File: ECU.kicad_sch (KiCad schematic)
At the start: 6 parts

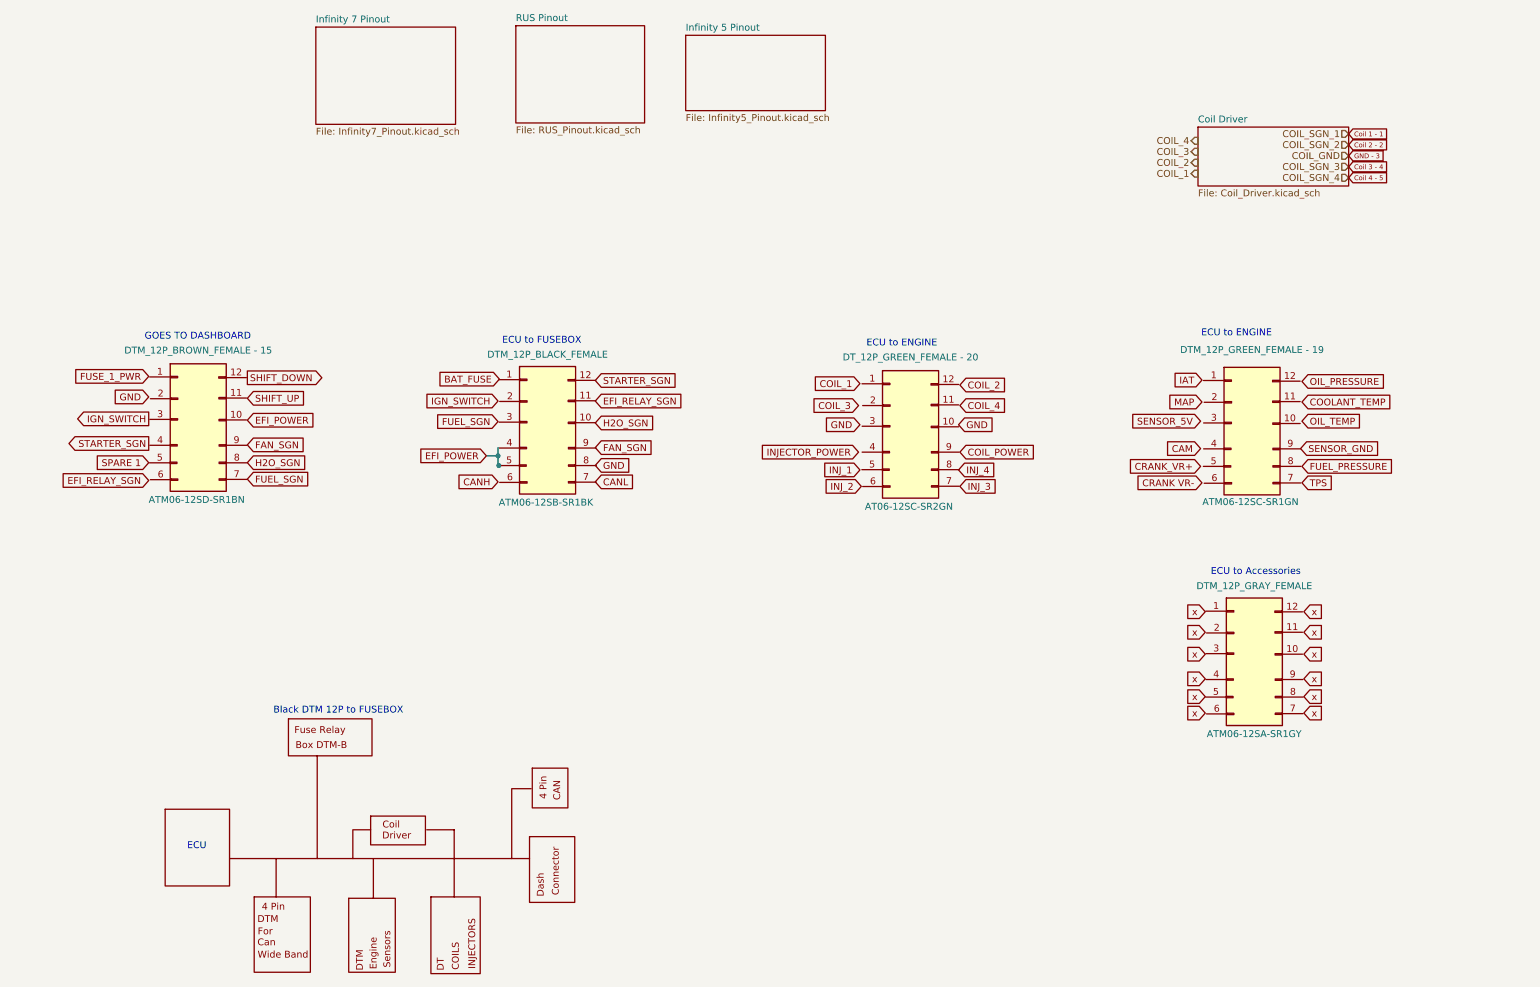
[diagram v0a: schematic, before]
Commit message: readd all connectors
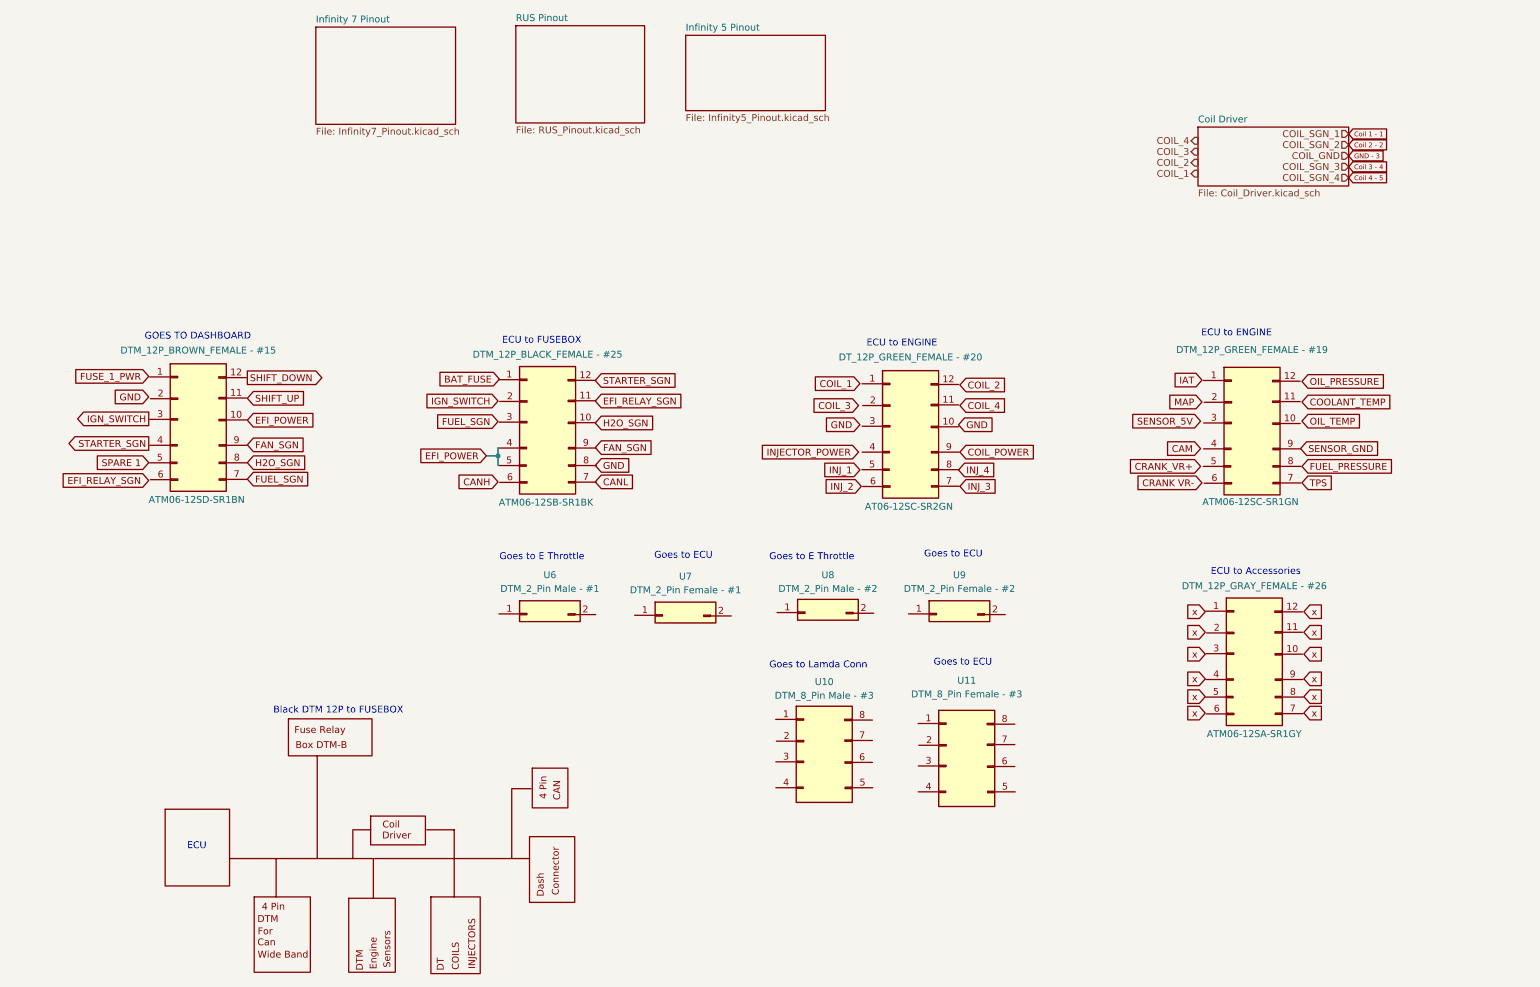
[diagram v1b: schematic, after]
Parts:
- added U10: DTM_8_Pin Male - #3, symbol SCR23 Library:DTM_8_Pin
- added U11: DTM_8_Pin Female - #3, symbol SCR23 Library:DTM_8_Pin
- added U6: DTM_2_Pin Male - #1, symbol SCR23 Library:DTM_2_Pin
- added U7: DTM_2_Pin Female - #1, symbol SCR23 Library:DTM_2_Pin
- added U8: DTM_2_Pin Male - #2, symbol SCR23 Library:DTM_2_Pin
- added U9: DTM_2_Pin Female - #2, symbol SCR23 Library:DTM_2_Pin
- U?: value DTM_12P_BROWN_FEMALE - 15 -> DTM_12P_BROWN_FEMALE - #15
- U?: value DTM_12P_GRAY_FEMALE -> DTM_12P_GRAY_FEMALE - #26
- U?: value DTM_12P_BLACK_FEMALE -> DTM_12P_BLACK_FEMALE - #25
- U?: value DTM_12P_GREEN_FEMALE - 19 -> DTM_12P_GREEN_FEMALE - #19
- U?: value DT_12P_GREEN_FEMALE - 20 -> DT_12P_GREEN_FEMALE - #20
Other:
- note added: "Goes to E Throttle"
- note added: "Goes to ECU"
- note added: "Goes to Lamda Conn"

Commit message: Updating Connectors
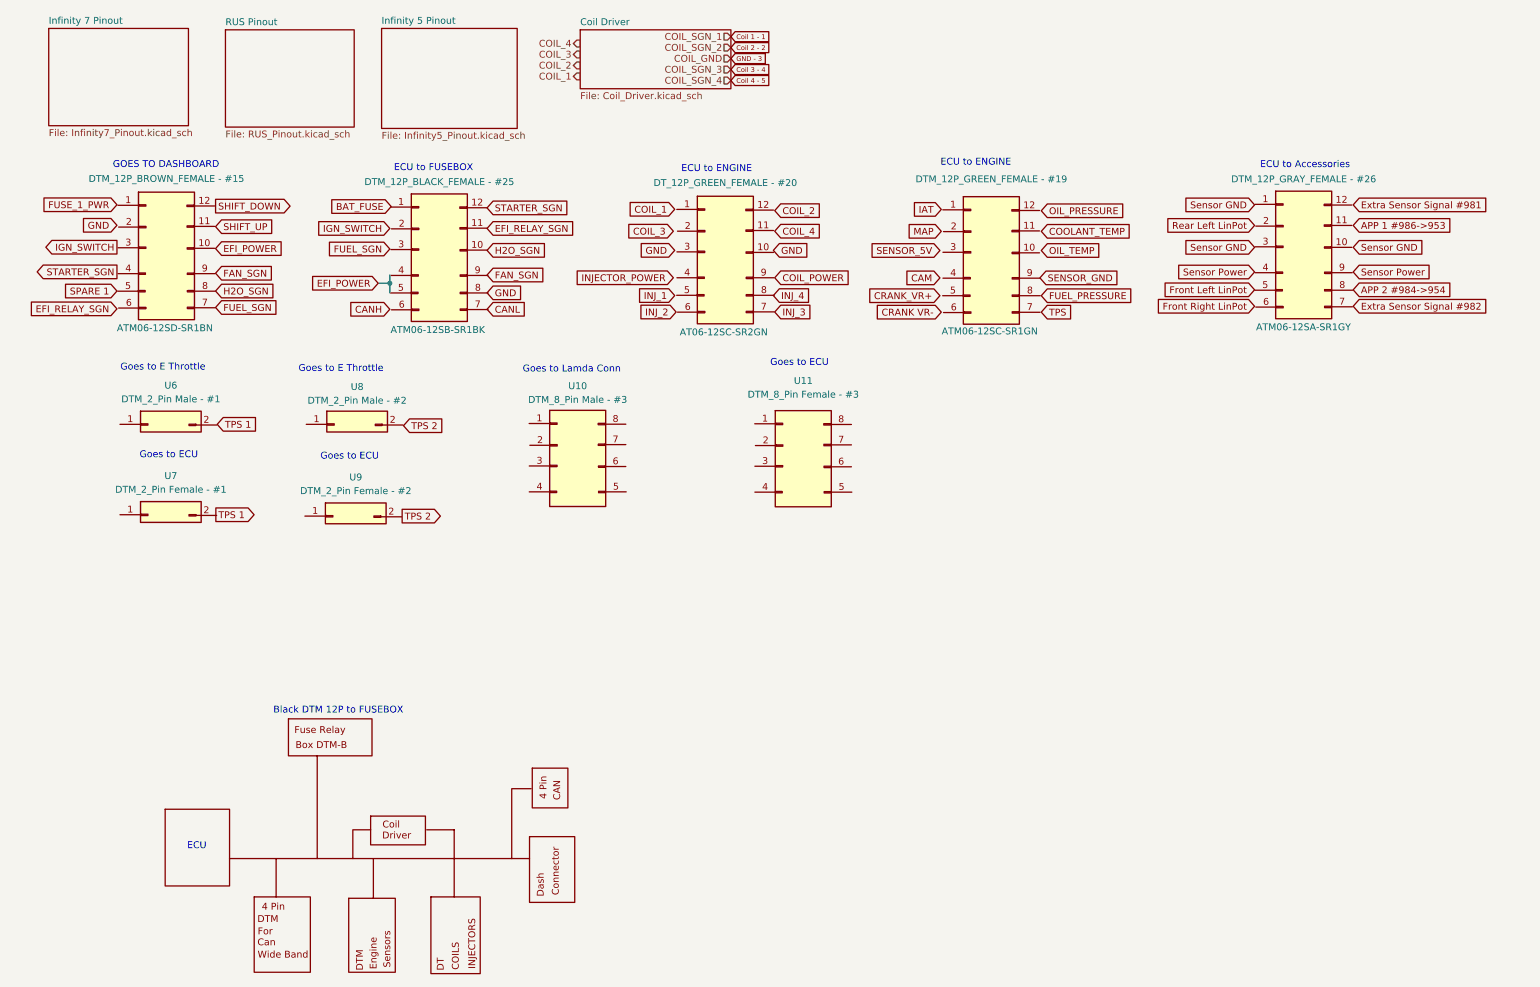
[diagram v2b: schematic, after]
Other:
- moved on the sheet: U10, U11, U6, U7, U8, U9
